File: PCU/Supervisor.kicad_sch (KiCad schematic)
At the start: 0 parts

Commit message: Supervisor Block
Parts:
- added C232, C239, C241, C247: 1uF 50V, Capacitor_SMD:C_0805_2012Metric, symbol Device:C
- added C233: 4.7uF 50V, Capacitor_SMD:C_1206_3216Metric, symbol Device:C
- added C234, C236: 12nF 50V 5%, Capacitor_SMD:C_0603_1608Metric, symbol Device:C
- added C238, C243, C244, C249, C252, C254: 0.1uF 50V, Capacitor_SMD:C_0603_1608Metric, symbol Device:C
- added C245, C246, C255: 15nF, Capacitor_SMD:C_0603_1608Metric, symbol Device:C
- added D51: PESD3V3S2UT,215, BassingaLib_TVS:SOT95P230X110-3N, symbol BassingaLib_TVS:PESD3V3S2UT,215
- added FL1: ECMF2-40A100N6, BassingaLib_ESD_Protection:ECMF240A100N6, symbol BassingaLib_ESD_Protection:ECMF2-40A100N6
- added IC36: TCAN3403DDFRQ1, BassinaLib_Com_Interfaces:SOT65P280X110-8N, symbol BassinaLib_Com_Interfaces:TCAN3403DDFRQ1
- added IC38: STM32G473CCT3, BassingaLib_MCU:QFP50P900X900X160-48N, symbol BassingaLib_MCU:STM32G473CCT3
- added J19: JST SH 5Pin, BassinaLib_Connectors:JST_BM05B-SRSS-TB_LF__SN_, symbol BassinaLib_Connectors:BM05B-SRSS-TB_LF__SN_
- added J20: JST SH 3Pin, BassinaLib_Connectors:JST_BM03B-SRSS-TB_LF__SN_, symbol BassinaLib_Connectors:BM03B-SRSS-TB_LF__SN_
- added J21: USB4120-03-C, BassinaLib_Connectors:USB412003C, symbol BassinaLib_Connectors:USB4120-03-C
- added LED21: GREEN, BassinaLib_LEDs:LEDM168X80N, symbol BassinaLib_LEDs:APHD1608LZGCK
- added LED22: BLUE, BassinaLib_LEDs:LEDM168X80N, symbol BassinaLib_LEDs:APHD1608LQBC_D
- added LED23: RED LED, BassinaLib_LEDs:LEDM168X80N, symbol BassinaLib_LEDs:APHD1608LSURCK
- added R271, R275, R278, R287, R288: 10k 1%, Resistor_SMD:R_0603_1608Metric, symbol Device:R
- added R281, R284: 1k 1%, Resistor_SMD:R_0603_1608Metric, symbol Device:R
- added R282, R283: 22R 1%, Resistor_SMD:R_0603_1608Metric, symbol Device:R
- added R285: 2k 1%, Resistor_SMD:R_0603_1608Metric, symbol Device:R
- added R286, R291: 5.1k 1%, Resistor_SMD:R_0603_1608Metric, symbol Device:R
- added R289: 33k 1%, Resistor_SMD:R_0603_1608Metric, symbol Device:R
- added R290: 68k 1%, Resistor_SMD:R_0603_1608Metric, symbol Device:R
- added TH5: NCU18XH103D60RB, Resistor_SMD:R_0603_1608Metric, symbol Device:Thermistor_NTC
- added TP12: TestPoint, TestPoint:TestPoint_Pad_D1.0mm, symbol Connector:TestPoint
- added Y5: ECS-80-10-30B-CWN-TR, BassinaLib_Crystals:ECS801830BAGNTR, symbol BassinaLib_Crystals:ECS-80-10-30B-CWN-TR
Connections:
- net EN_Precharge: now also IC38.27 (PB13)
- net EN_mainBus: now also IC38.28 (PB14)
- net V12Logic_Mesure: now also IC38.9 (PA1)
- net V12_Mesure: now also IC38.14 (PA6)
- net V3.3Logic_Mesure: now also IC38.11 (PA3)
- net V3.3_Mesure: now also IC38.15 (PA7)
- net V5Logic_Mesure: now also IC38.10 (PA2)
- net Vbat_Mesure: now also IC38.8 (PA0)
- net Vbus_Mesure: now also IC38.13 (PA5)
- net mainBus_nFault: now also IC38.29 (PB15)
- new net: J21.A5 (CC1), R286.1
- new net: J21.B5 (CC2), R291.1
- new net: LED23.2 (A), R285.2
- new net: IC38.2 (PC13), R275.2, TP12.1
- new net: IC38.45 (PB8-BOOT0), R278.2
- new net: LED21.2 (A), R281.2
- new net: J20.1, R282.1
- new net: J20.3, R283.1
- new net: LED22.2 (A), R284.2
- new net +3.3V_Logic: C232.1, C233.1, C239.1, C241.2, C243.2, C244.2, C245.2, C246.2, C247.2, C249.2, C252.1, IC36.3 (V_CC), IC36.5 (VIO), IC38.20 (VREF+), IC38.21 (VDDA), IC38.24 (VDD_1), IC38.36 (VDD_2), IC38.48 (VDD_3), J19.1, R271.1, R287.1, TH5.1
- new net Blue_LED: IC38.25 (PB11), R284.1
- new net D_N: FL1.5 (D-_TO_IC), IC38.33 (PA11)
- new net D_P: FL1.6 (D+_TO_IC), IC38.34 (PA12)
- new net Dx_N: FL1.2 (D-_TO_CONNECTOR), J21.A7 (DN1), J21.B7 (DN2)
- new net Dx_P: FL1.1 (D+_TO_CONNECTOR), J21.A6 (DP1), J21.B6 (DP2)
- new net FDCAN3_RX: IC36.4 (RXD), IC38.40 (PB3)
- new net FDCAN3_STB: IC36.8 (STB), IC38.42 (PB5)
- new net FDCAN3_TX: IC36.1 (TXD), IC38.41 (PB4)
- new net GND: C232.2, C233.2, C234.1, C236.1, C238.1, C239.2, C241.1, C243.1, C244.1, C245.1, C246.1, C247.1, C249.1, C252.2, C254.1, C255.1, D51.3, FL1.3 (GND_1), FL1.4 (GND_2), IC36.2 (GND), IC38.19 (VSSA), IC38.23 (VSS_1), IC38.35 (VSS_2), IC38.47 (VSS_3), J19.5, J19.S1 (SHIELD), J19.S2 (SHIELD), J20.2, J20.S1 (SHIELD), J20.S2 (SHIELD), J21.A1 (GND_1), J21.A12 (GND_2), J21.B1 (GND_3), J21.B12 (GND_4), J21.MH1, J21.MH2, J21.MH3, J21.MH4, LED21.1 (K), LED22.1 (K), LED23.1 (K), R275.1, R278.1, R286.2, R288.2, R290.1, R291.2, Y5.2, Y5.4
- new net Green_LED: IC38.22 (PB10), R281.1
- new net OSC1: C234.2, IC38.5 (PF0_-_OSC_IN), Y5.1
- new net OSC2: C236.2, IC38.6 (PF1_-_OSC_OUT), Y5.3
- new net PCB_Temp: C255.2, IC38.30 (PA8), R287.2, R288.1, TH5.2
- new net Red_LED: IC38.26 (PB12), R285.1
- new net SPV_CANH: IC36.7 (CANH)
- new net SPV_CANL: IC36.6 (CANL)
- new net SWCLK: IC38.38 (PA14), J19.3
- new net SWDIO: IC38.37 (PA13), J19.2
- new net UART1_RX: D51.1, IC38.44 (PB7), R282.2
- new net UART1_TX: D51.2, IC38.43 (PB6), R283.2
- new net USB_Vbus: IC38.32 (PA10), R289.1, R290.2
- new net USBx_Vbus: C254.2, J21.A4 (VBUS_1), J21.A9 (VBUS_2), J21.B4 (VBUS_3), J21.B9 (VBUS_4), R289.2
- new net nRST: C238.2, IC38.7 (PG10_-_NRST), J19.4, R271.2
- no-connect marks 0 -> 12
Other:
- note added: "FD-CAN Interface"
- note added: "PCB Temperature Mesurement"
- note added: "Programming Interface (SWD)"
- note added: "UART Interface"
- note added: "USB 2.0 Interface"

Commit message: End of schematic
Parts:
- added C256: 0.1uF 50V, Capacitor_SMD:C_0603_1608Metric, symbol Device:C
- added S2, S3: TS04-66-43-BK-260-SMT, BassingaLib_Button:TS046643BK260SMT, symbol BassingaLib_Button:TS04-66-43-BK-260-SMT
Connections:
- net GND: now also C256.1, S2.2, S2.4, S3.2, S3.4
- net nRST: now also S2.1, S2.3
- net push_button: now reaches IC38.12 (PA4)
- net push_button: now also C256.2, S3.1, S3.3
- no-connect marks 12 -> 11
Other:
- moved on the sheet: C233

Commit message: Start of PCB Design
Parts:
- added R265: 10k 1%, Resistor_SMD:R_0603_1608Metric, symbol Device:R
- renumbered C234 to C233, C256 to C234, C233 to C254, C254 to C255, C255 to C256, R271 to R272, R275 to R276, R278 to R279, R281 to R282, R282 to R283, R283 to R284, R284 to R285, R285 to R286, R286 to R287, R287 to R288, R288 to R289, R289 to R290, R290 to R291, R291 to R292, S3 to S2, S2 to S3
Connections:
- net +3.3V_Logic: now also R265.1
- net GND: no longer S2.2, S2.4
- new net: R265.2, S2.2, S2.4

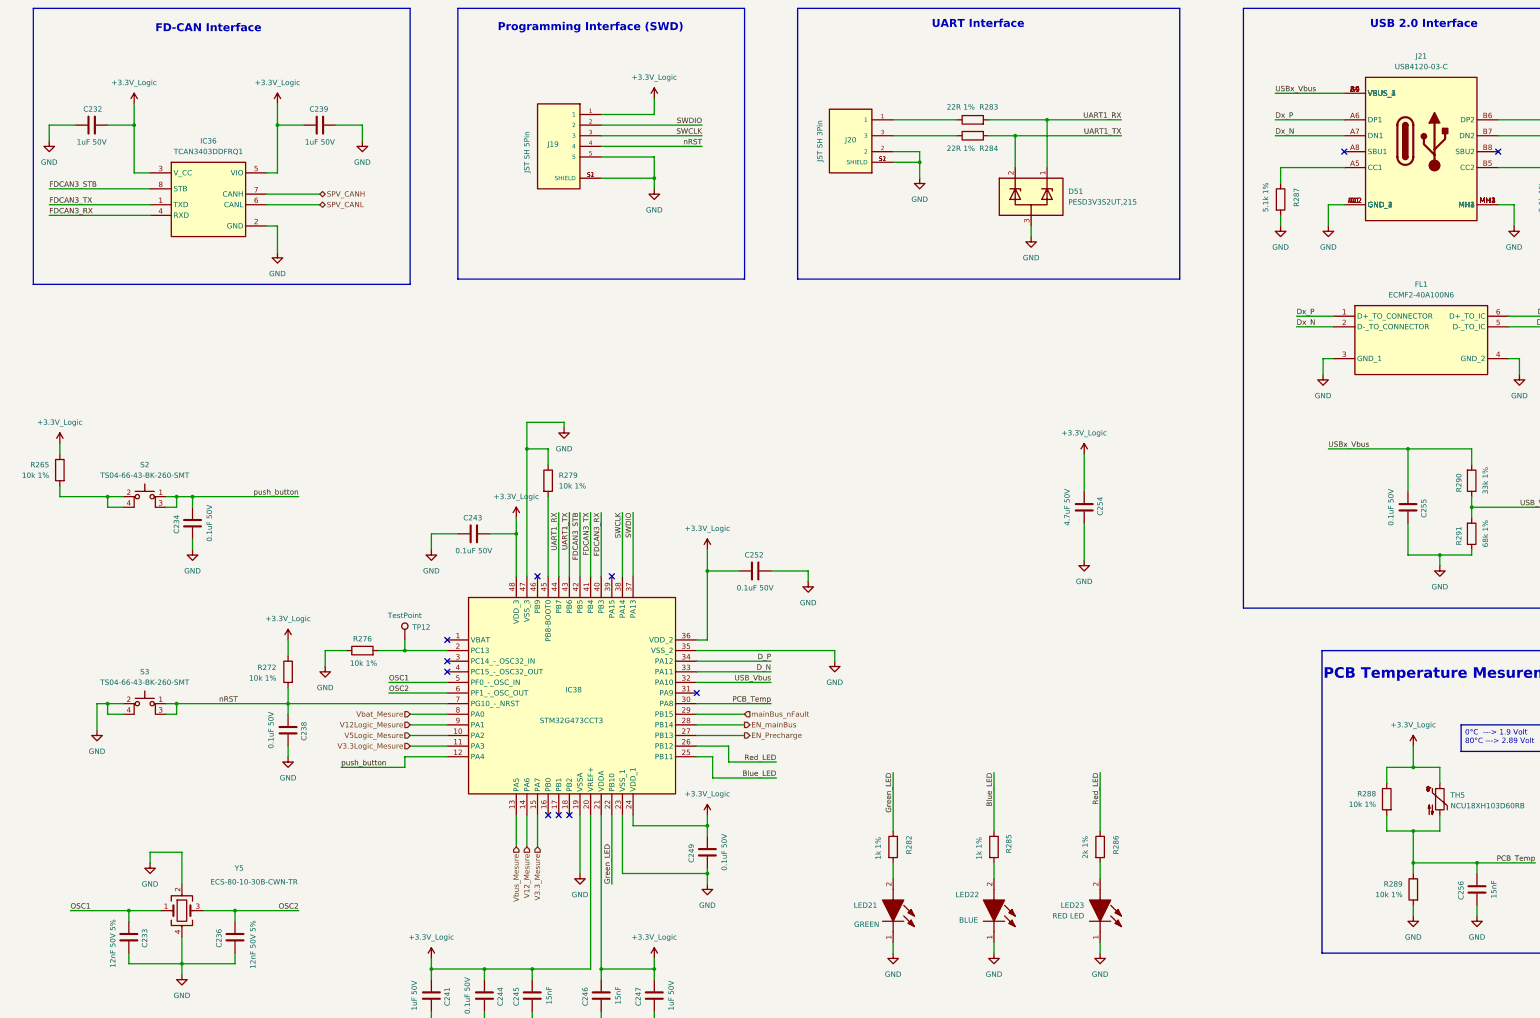
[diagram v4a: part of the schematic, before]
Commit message: PSU Blocks Routed
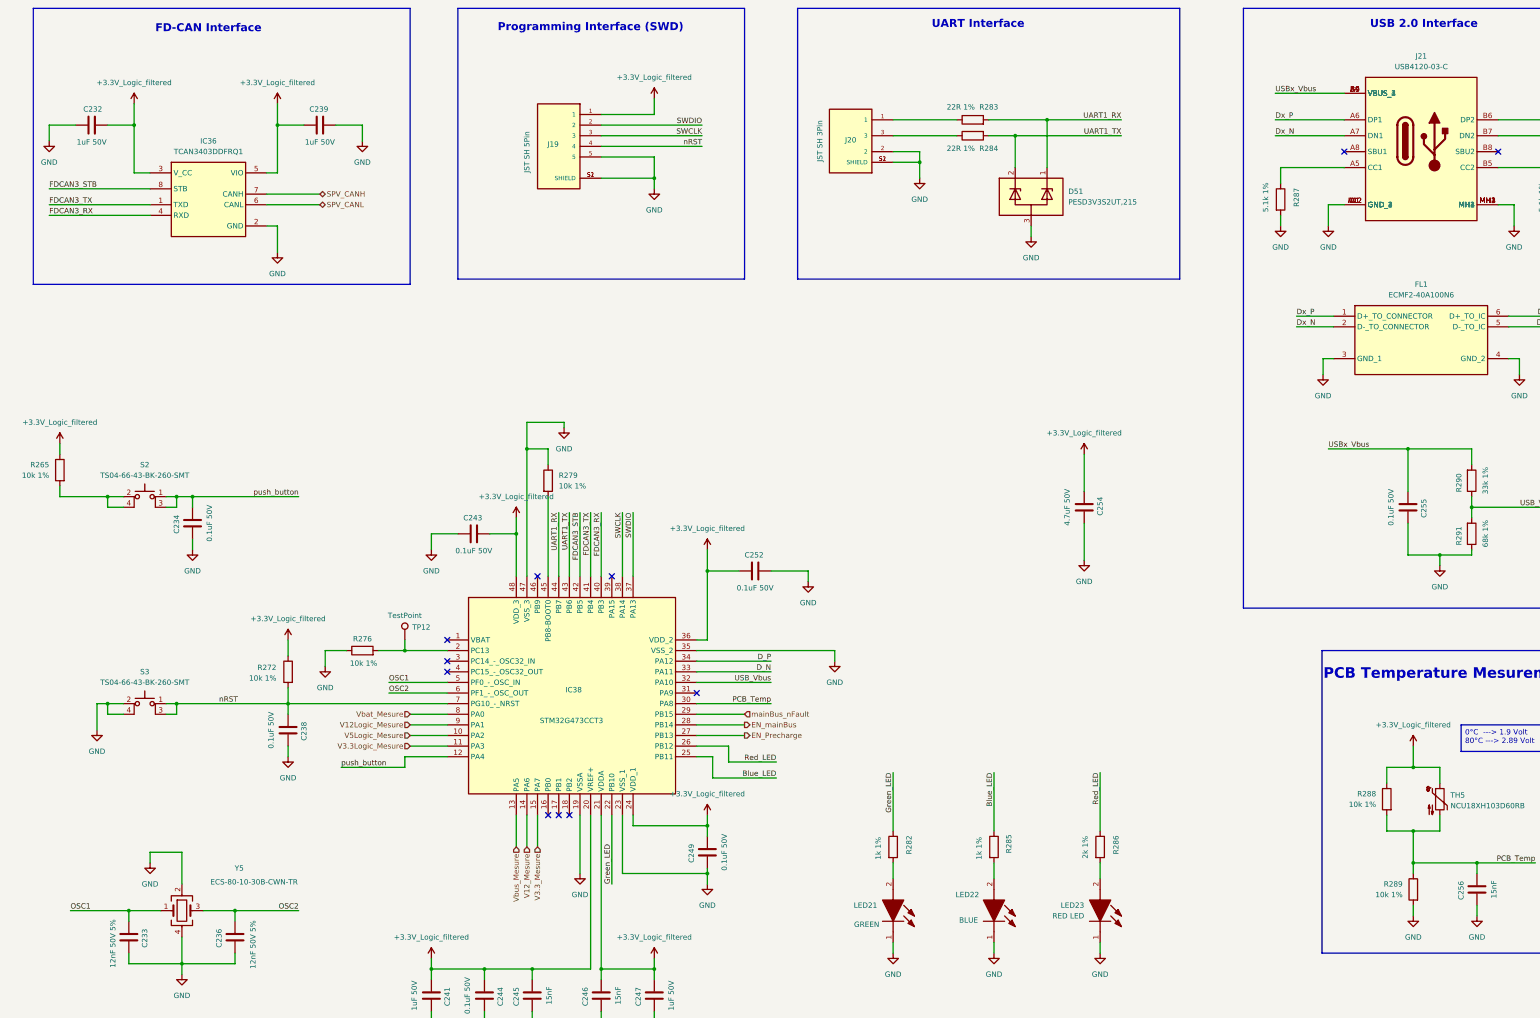
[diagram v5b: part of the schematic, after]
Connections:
- net +3.3V_Logic renamed +3.3V_Logic_filtered
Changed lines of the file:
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@@
 			)
 		)
-		(property "Value" "+3.3V_Logic"
+		(property "Value" "+3.3V_Logic_filtered"
 			(at 44.45 34.29 0)
 			(effects
@@
 			)
 		)
-		(property "Value" "+3.3V_Logic"
+		(property "Value" "+3.3V_Logic_filtered"
 			(at 181.61 140.97 0)
 			(effects
@@
 			)
 		)
-		(property "Value" "+3.3V_Logic"
+		(property "Value" "+3.3V_Logic_filtered"
 			(at 168.91 33.02 0)
 			(effects
@@
 			)
 		)
-		(property "Value" "+3.3V_Logic"
+		(property "Value" "+3.3V_Logic_filtered"
 			(at 168.91 238.76 0)
 			(effects
@@
 			)
 		)
-		(property "Value" "+3.3V_Logic"
+		(property "Value" "+3.3V_Logic_filtered"
 			(at 271.78 118.11 0)
 			(effects
@@
 			)
 		)
-		(property "Value" "+3.3V_Logic"
+		(property "Value" "+3.3V_Logic_filtered"
 			(at 350.52 187.96 0)
 			(effects
@@
 			)
 		)
-		(property "Value" "+3.3V_Logic"
+		(property "Value" "+3.3V_Logic_filtered"
 			(at 81.28 162.56 0)
 			(effects
@@
 			)
 		)
-		(property "Value" "+3.3V_Logic"
+		(property "Value" "+3.3V_Logic_filtered"
 			(at 181.61 204.47 0)
 			(effects
@@
 			)
 		)
-		(property "Value" "+3.3V_Logic"
+		(property "Value" "+3.3V_Logic_filtered"
 			(at 26.67 115.57 0)
 			(effects
@@
 			)
 		)
-		(property "Value" "+3.3V_Logic"
+		(property "Value" "+3.3V_Logic_filtered"
 			(at 78.74 34.29 0)
 			(effects
@@
 			)
 		)
-		(property "Value" "+3.3V_Logic"
+		(property "Value" "+3.3V_Logic_filtered"
 			(at 115.57 238.76 0)
 			(effects
@@
 			)
 		)
-		(property "Value" "+3.3V_Logic"
+		(property "Value" "+3.3V_Logic_filtered"
 			(at 135.89 133.35 0)
 			(effects

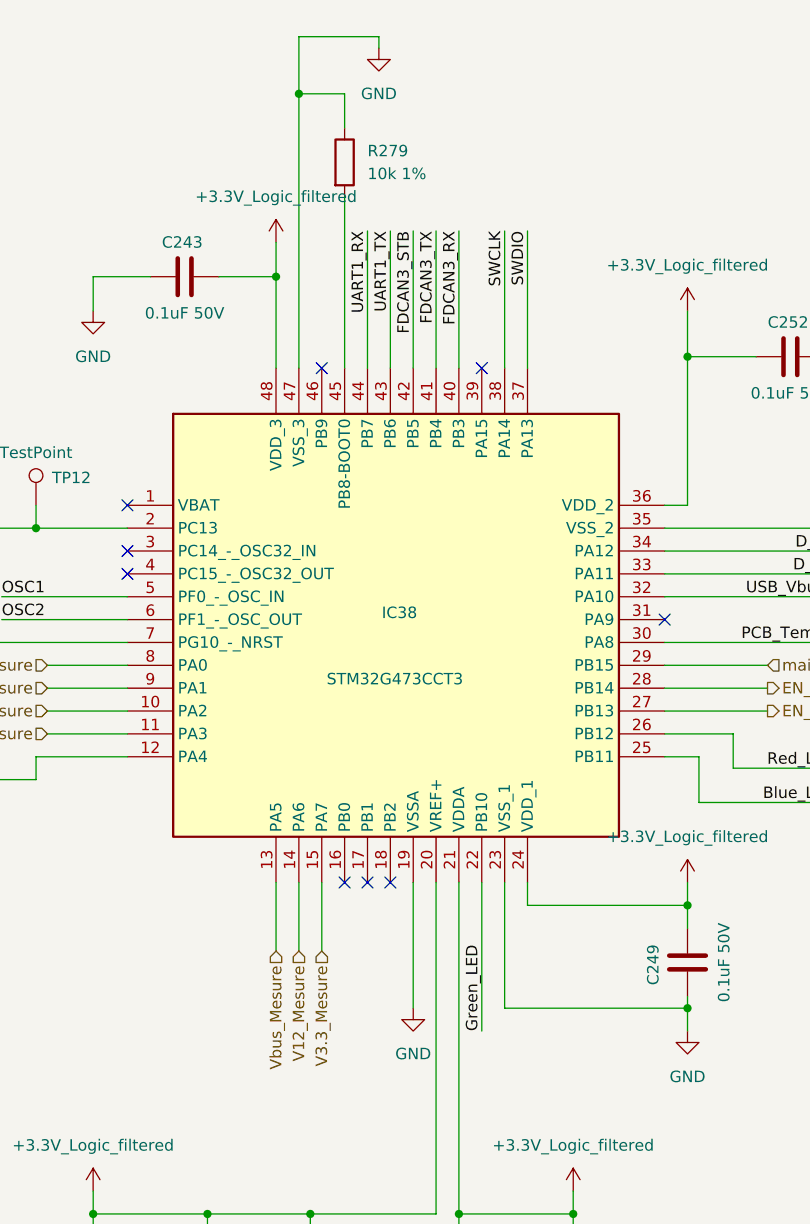
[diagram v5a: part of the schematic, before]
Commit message: ESCs Analog signals routed
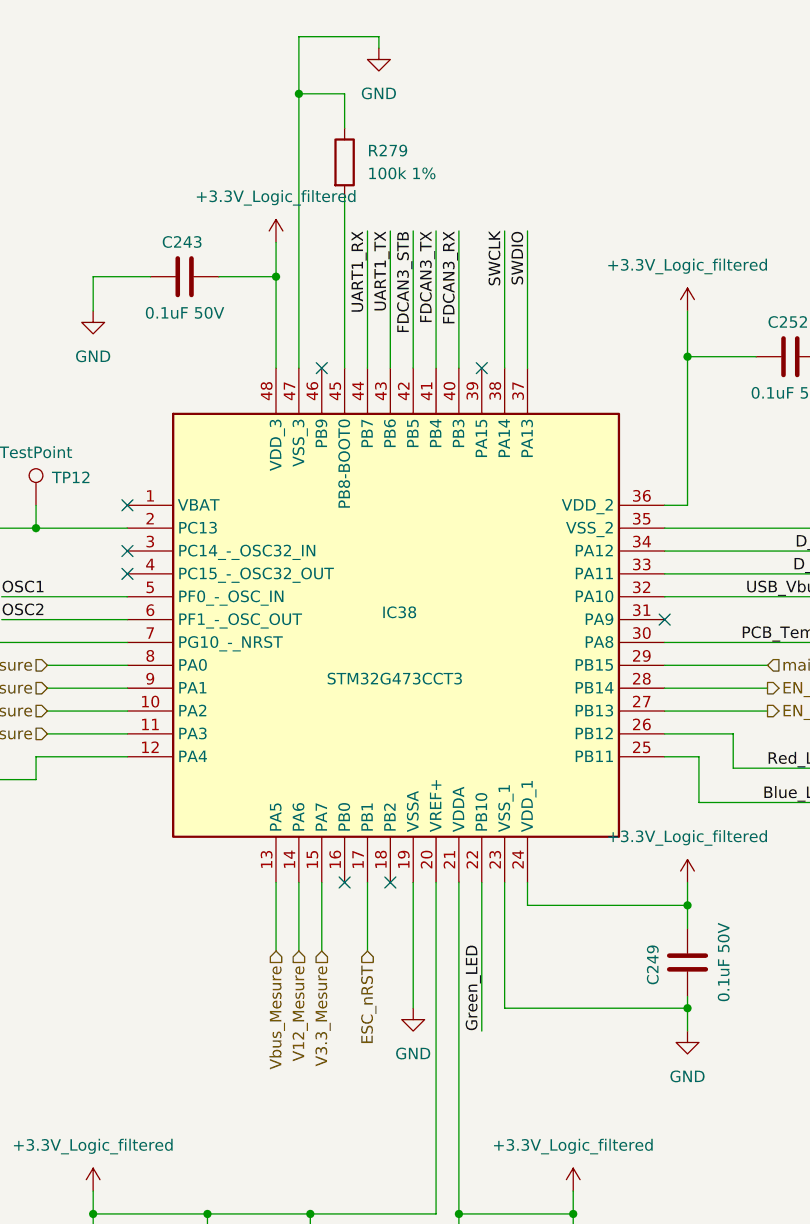
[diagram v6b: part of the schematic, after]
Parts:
- R279: value 10k 1% -> 100k 1%; Manufacturer_Part_Number AF0603FR-0710KL -> AT0603FRE07100KL
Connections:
- net ESC_nRST: now reaches IC38.17 (PB1)
- no-connect marks 11 -> 10
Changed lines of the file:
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@@
 	)
 	(no_connect
-		(at 143.51 209.55)
-	)
-	(no_connect
-		(at 146.05 209.55)
-	)
-	(no_connect
 		(at 370.84 50.8)
 	)
@@
 		(at 334.01 50.8)
 	)
+	(no_connect
+		(at 143.51 209.55)
+	)
 	(wire
 		(pts
@@
 	(wire
 		(pts
+			(xy 146.05 209.55) (xy 146.05 217.17)
+		)
+		(stroke
+			(width 0)
+			(type default)
+		)
+	)
+	(wire
+		(pts
 			(xy 181.61 151.13) (xy 189.23 151.13)
 		)
@@
 		)
 	)
+	(hierarchical_label "ESC_nRST"
+		(shape input)
+		(at 146.05 217.17 270)
+		(effects
+			(font
+				(size 1.27 1.27)
+			)
+			(justify right)
+		)
+	)
 	(hierarchical_label "EN_Precharge"
 		(shape output)
@@
 			)
 		)
-		(property "Value" "10k 1%"
+		(property "Value" "100k 1%"
 			(at 146.05 130.8099 0)
 			(effects
@@
 			)
 		)
-		(property "Manufacturer_Part_Number" "AF0603FR-0710KL"
+		(property "Manufacturer_Part_Number" "AT0603FRE07100KL"
 			(at 143.51 129.54 0)
 			(effects

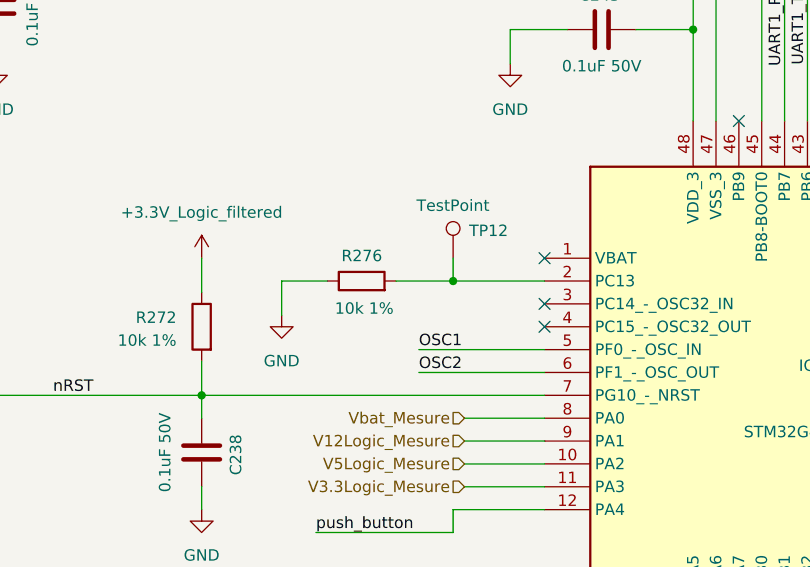
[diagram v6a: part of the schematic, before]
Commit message: All analog signals routed
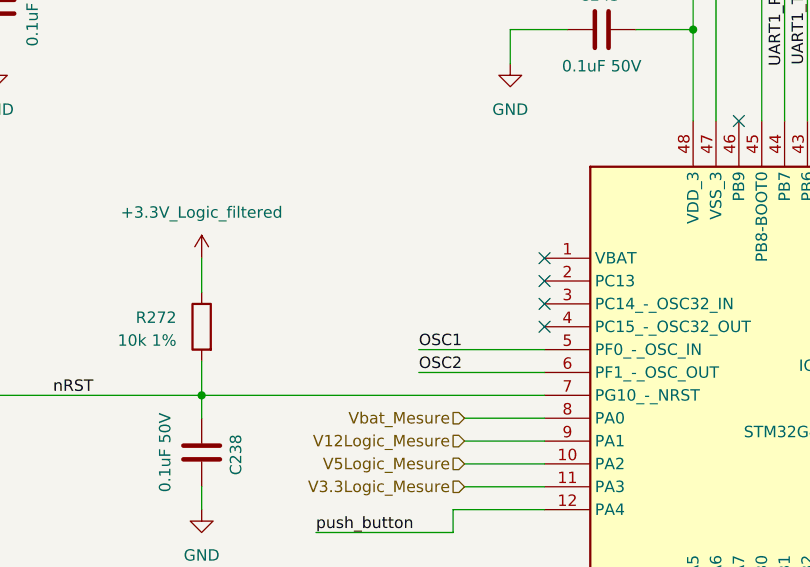
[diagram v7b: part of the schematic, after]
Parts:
- removed R276: 10k 1%, Resistor_SMD:R_0603_1608Metric, symbol Device:R
- removed TP12: TestPoint, TestPoint:TestPoint_Pad_D1.0mm, symbol Connector:TestPoint
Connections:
- no-connect marks 10 -> 11
